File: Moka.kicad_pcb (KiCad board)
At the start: 2 copper layers, 60 x 60 mm, 66 parts, among them J1 CONN_02X03, J10 CONN_01X05, J2 GS2, J3 GS2, J4 GS2, J5 GS2, J6 GS2, J7 CONN_01X05, J8 CONN_01X05, J9 CONN_01X05, SW1 SW_Push, SW10 SW_Push, SW11 SW_Push, SW12 SW_Push, SW13 SW_Push, SW14 SW_Push, SW15 SW_Push, SW16 SW_Push, SW2 SW_Push, SW3 SW_Push, SW4 SW_Push, SW5 SW_Push, SW6 SW_Push, SW7 SW_Push, SW8 SW_Push, SW9 SW_Push, U1 ATMEGA328P-AU

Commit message: Design ok, first prototype batch ordered.
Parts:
- added logo1: Moka, Logos:Moka_20mm, B.Cu at (180.6, 128.2)
- added logo2: le labo, Logos:Le_labo_15mm, B.Cu at (151.2, 128.9)
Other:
- board text added: "6/2017"
- board text added: "lelabodutroisieme.fr"
- board text added: "v0.9"

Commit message: v0.95 ready for fabrication.
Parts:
- added D17: SK6812_MINI, Display_perso:SK6812-mini, F.Cu at (187.5, 132.5)
- D1: value Led_3535_addr -> D; footprint Display_perso:SK6812-mini -> Diodes_SMD:D_0603; moved to B.Cu
- D10, D11, D12, D13, D14, D15, D16, D2, D3, D4, D5, D6, D7, D8, D9: value Led_3535_addr -> SK6812_MINI
- J1: value CONN_02X03 -> Conn_02x03_Odd_Even; footprint Conn_perso:Pin_Header_Straight_2x03_Pitch2.54mm_SMD -> Connectors_perso:Pin_Header_Straight_2x03_Pitch2.54mm_SMD
- J10, J7, J8, J9: footprint Conn_perso:Connecteur_1x5_SMD -> Connectors_perso:Connecteur_1x5_SMD
- SW1, SW10, SW11, SW12, SW13, SW14, SW15, SW16, SW2, SW3, SW4, SW5, SW6, SW7, SW8, SW9: footprint Switches_perso:Pad_30 -> switches_perso:Pad_30
- logo1: footprint Logos:Moka_20mm -> logos:Moka_25mm
- logo2: footprint Logos:Le_labo_15mm -> logos:Le_labo_20mm
- moved J8 56.0 mm to (165.0, 138.0)
- moved D13 47.4 mm to (187.5, 117.5)
- moved D5 47.4 mm to (187.5, 87.5)
- moved D9 47.4 mm to (187.5, 102.5)
- moved J10 39.6 mm to (193.0, 110.0), turned to 90 degrees
- moved J9 39.6 mm to (165.0, 82.0), turned to 0 degrees
- moved D1 38.2 mm to (169.2, 114.8), turned to 315 degrees
- moved C3 37.1 mm to (190.1, 111.3), turned to 90 degrees
- moved C4 35.5 mm to (163.8, 135.0), turned to 0 degrees
- moved J2 35.0 mm to (180.1, 115.1), turned to 270 degrees
- moved C2 34.9 mm to (163.7, 84.9), turned to 0 degrees
- moved C5 33.8 mm to (140.0, 111.3), turned to 90 degrees
- moved J3 33.4 mm to (180.1, 112.6), turned to 270 degrees
- moved J4 32.1 mm to (180.1, 110.1), turned to 270 degrees
- moved J5 31.1 mm to (180.1, 107.5), turned to 270 degrees
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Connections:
- D1 pad 1: GND -> Net-(D1-Pad1)
- D1 pad 2: DIN -> INT
- D10 pad 1: GND -> Net-(D10-Pad1)
- D10 pad 2: Net-(D10-Pad2) -> GND
- D10 pad 3: +5V -> Net-(D10-Pad3)
- D10 pad 4: Net-(D10-Pad4) -> +5V
- D11 pad 1: GND -> Net-(D11-Pad1)
- D11 pad 2: Net-(D10-Pad4) -> GND
- D11 pad 3: +5V -> Net-(D10-Pad1)
- D11 pad 4: Net-(D11-Pad4) -> +5V
- D12 pad 1: GND -> Net-(D12-Pad1)
- D12 pad 2: Net-(D11-Pad4) -> GND
- D12 pad 3: +5V -> Net-(D11-Pad1)
- D12 pad 4: Net-(D12-Pad4) -> +5V
- D13 pad 1: GND -> Net-(D13-Pad1)
- D13 pad 2: Net-(D12-Pad4) -> GND
- D13 pad 3: +5V -> Net-(D12-Pad1)
- D13 pad 4: Net-(D13-Pad4) -> +5V
- D14 pad 1: GND -> Net-(D14-Pad1)
- D14 pad 2: Net-(D13-Pad4) -> GND
- D14 pad 3: +5V -> Net-(D13-Pad1)
- D14 pad 4: Net-(D14-Pad4) -> +5V
- D15 pad 1: GND -> Net-(D15-Pad1)
- D15 pad 2: Net-(D14-Pad4) -> GND
- D15 pad 3: +5V -> Net-(D14-Pad1)
- D15 pad 4: Net-(D15-Pad4) -> +5V
- D16 pad 1: GND -> Net-(D16-Pad1)
- D16 pad 2: Net-(D15-Pad4) -> GND
- D16 pad 3: +5V -> Net-(D15-Pad1)
- D16 pad 4: (no net) -> +5V
- D2 pad 1: GND -> Net-(D2-Pad1)
- D2 pad 2: Net-(D1-Pad4) -> GND
- D2 pad 3: +5V -> DIN
- D2 pad 4: Net-(D2-Pad4) -> +5V
- D3 pad 1: GND -> Net-(D3-Pad1)
- D3 pad 2: Net-(D2-Pad4) -> GND
- D3 pad 3: +5V -> Net-(D2-Pad1)
- D3 pad 4: Net-(D3-Pad4) -> +5V
- D4 pad 1: GND -> Net-(D4-Pad1)
- D4 pad 2: Net-(D3-Pad4) -> GND
- D4 pad 3: +5V -> Net-(D3-Pad1)
- D4 pad 4: Net-(D4-Pad4) -> +5V
- D5 pad 1: GND -> Net-(D5-Pad1)
- D5 pad 2: Net-(D4-Pad4) -> GND
- D5 pad 3: +5V -> Net-(D4-Pad1)
- D5 pad 4: Net-(D5-Pad4) -> +5V
- D6 pad 1: GND -> Net-(D6-Pad1)
- D6 pad 2: Net-(D5-Pad4) -> GND
- D6 pad 3: +5V -> Net-(D5-Pad1)
- D6 pad 4: Net-(D6-Pad4) -> +5V
- D7 pad 1: GND -> Net-(D7-Pad1)
- D7 pad 2: Net-(D6-Pad4) -> GND
- D7 pad 3: +5V -> Net-(D6-Pad1)
- D7 pad 4: Net-(D7-Pad4) -> +5V
- D8 pad 1: GND -> Net-(D8-Pad1)
- D8 pad 2: Net-(D7-Pad4) -> GND
- D8 pad 3: +5V -> Net-(D7-Pad1)
- D8 pad 4: Net-(D8-Pad4) -> +5V
- D9 pad 1: GND -> Net-(D10-Pad3)
- D9 pad 2: Net-(D8-Pad4) -> GND
- D9 pad 3: +5V -> Net-(D8-Pad1)
- D9 pad 4: Net-(D10-Pad2) -> +5V
- SW1 pad 1: BOUT1 -> BREAD1
- SW1 pad 2: BIN1 -> BCH1
- SW10 pad 1: BOUT2 -> BREAD2
- SW10 pad 2: BIN3 -> BCH3
- SW11 pad 1: BOUT3 -> BREAD3
- SW11 pad 2: BIN3 -> BCH3
- SW12 pad 1: BOUT4 -> BREAD4
- SW12 pad 2: BIN3 -> BCH3
- SW13 pad 1: BOUT1 -> BREAD1
- SW13 pad 2: BIN4 -> BCH4
- SW14 pad 1: BOUT2 -> BREAD2
- SW14 pad 2: BIN4 -> BCH4
- SW15 pad 1: BOUT3 -> BREAD3
- SW15 pad 2: BIN4 -> BCH4
- SW16 pad 1: BOUT4 -> BREAD4
- SW16 pad 2: BIN4 -> BCH4
- SW2 pad 1: BOUT2 -> BREAD2
- SW2 pad 2: BIN1 -> BCH1
- SW3 pad 1: BOUT3 -> BREAD3
- SW3 pad 2: BIN1 -> BCH1
- SW4 pad 1: BOUT4 -> BREAD4
- SW4 pad 2: BIN1 -> BCH1
- SW5 pad 1: BOUT1 -> BREAD1
- SW5 pad 2: BIN2 -> BCH2
- SW6 pad 1: BOUT2 -> BREAD2
- SW6 pad 2: BIN2 -> BCH2
- SW7 pad 1: BOUT3 -> BREAD3
- SW7 pad 2: BIN2 -> BCH2
- SW8 pad 1: BOUT4 -> BREAD4
- SW8 pad 2: BIN2 -> BCH2
- SW9 pad 1: BOUT1 -> BREAD1
- SW9 pad 2: BIN3 -> BCH3
- U1 pad 1: DIN -> BCH4
- U1 pad 10: BOUT3 -> ADDR2
- U1 pad 11: BOUT4 -> ADDR3
- U1 pad 12: ADDR0 -> ADDR4
- U1 pad 13: ADDR1 -> DIN
- U1 pad 14: ADDR2 -> Net-(D1-Pad1)
- U1 pad 2: BOUT1 -> ADDR0
- U1 pad 23: BIN1 -> BREAD1
- U1 pad 24: BIN2 -> BREAD2
- U1 pad 25: BIN3 -> BREAD3
- U1 pad 26: BIN4 -> BREAD4
- U1 pad 30: ADDR3 -> BCH1
- U1 pad 31: ADDR4 -> BCH2
- U1 pad 32: INT -> BCH3
- U1 pad 9: BOUT2 -> ADDR1
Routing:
- net GND: track 438.9 -> 514.0 mm, vias 56 -> 57
- net BOUT1: track 70.4 -> 0.00 mm, vias 7 -> 0
- net BCH1: track 0.00 -> 70.3 mm, vias 0 -> 1
- net Net-(D4-Pad4): track 69.7 -> 0.00 mm, vias 2 -> 0
- net Net-(D8-Pad4): track 67.4 -> 0.00 mm, vias 4 -> 0
- net BOUT4: track 67.0 -> 0.00 mm, vias 7 -> 0
- net BIN1: track 65.5 -> 0.00 mm, vias 3 -> 0
- net BIN4: track 62.9 -> 0.00 mm, vias 4 -> 0
- net BCH4: track 0.00 -> 61.3 mm, vias 0 -> 3
- net Net-(D10-Pad3): track 0.00 -> 60.8 mm, vias 0 -> 2
- net Net-(D12-Pad4): track 57.7 -> 0.00 mm, vias 2 -> 0
- net Net-(D5-Pad1): track 0.00 -> 55.7 mm, vias 0 -> 2
- net BOUT2: track 55.1 -> 0.00 mm, vias 5 -> 0
- net BOUT3: track 54.9 -> 0.00 mm, vias 7 -> 0
- net BCH3: track 0.00 -> 54.0 mm, vias 0 -> 1
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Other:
- board text added: "9/2017"
- board text added: "ADDR0"
- board text added: "ADDR1"
- board text added: "ADDR2"
- board text added: "ADDR3"
- board text added: "ADDR4"
- board text added: "MISO"
- board text added: "MOSI"
- board text added: "RST"
- board text added: "SCK"
- board text added: "v0.95"
- board text removed: "6/2017"
- board text removed: "addr 0"
- board text removed: "addr 1"
- board text removed: "addr 2"
- board text removed: "addr 3"
- board text removed: "addr 4"
- board text removed: "v0.9"

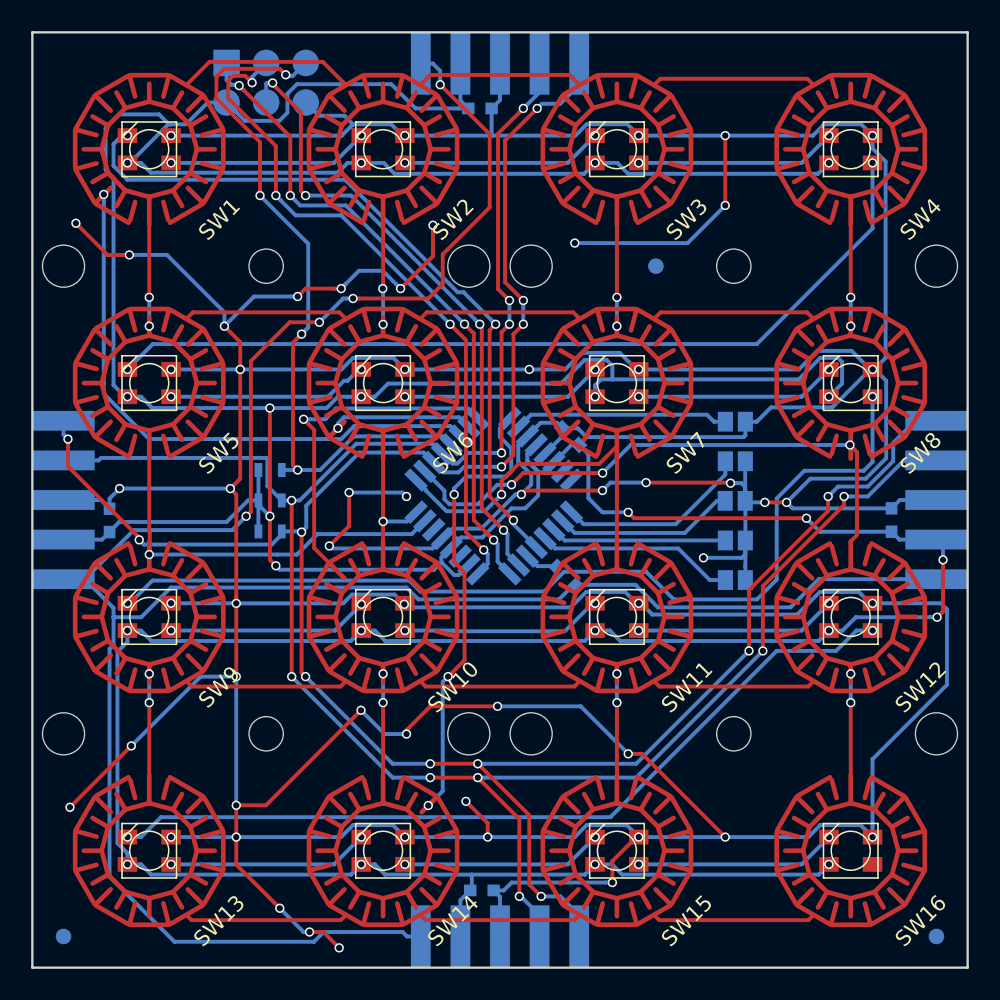
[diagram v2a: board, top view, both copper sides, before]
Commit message: Modified diode footprint on INT.
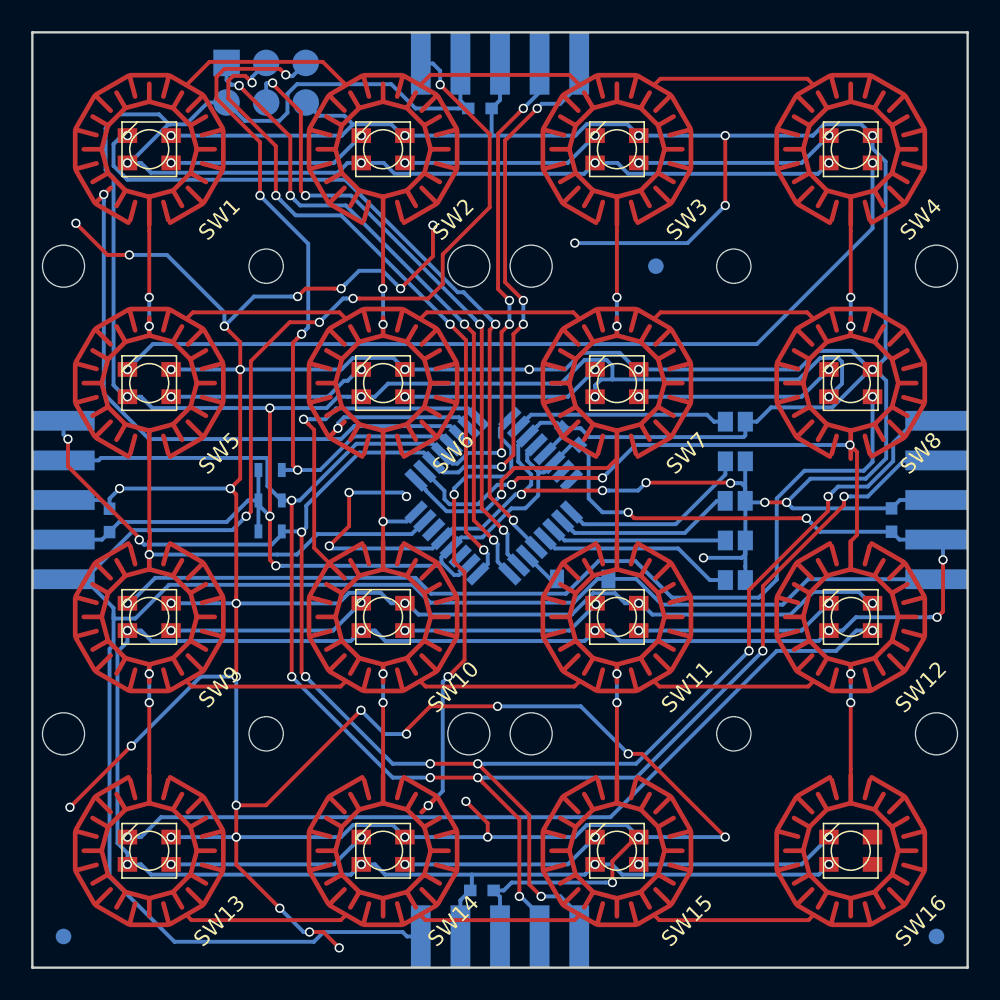
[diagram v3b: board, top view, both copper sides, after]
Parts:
- D1: footprint Diodes_SMD:D_0603 -> Diodes_SMD:D_SOD-123
- moved D1 1.13 mm to (170.3, 115.1), turned to 0 degrees
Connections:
- D17 pad 1: (no net) -> Net-(D17-Pad1)
- U1 pad 19: (no net) -> Net-(U1-Pad19)
- U1 pad 22: (no net) -> Net-(U1-Pad22)
- U1 pad 7: (no net) -> Net-(U1-Pad7)
- U1 pad 8: (no net) -> Net-(U1-Pad8)
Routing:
- net GND: track 514.0 -> 482.8 mm, vias 57 -> 56
- net Net-(D10-Pad3): track 60.8 -> 61.6 mm
- net INT: track 153.2 -> 153.7 mm

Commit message: Added missing via on last led raw GND.
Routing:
- net GND: vias 56 -> 57
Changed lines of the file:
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@@
     (links 858)
     (no_connects 721)
-    (area 134.924999 79.924999 195.075001 140.075001)
+    (area 131.680952 74.578618 198.319048 142.885)
     (thickness 1.6)
     (drawings 39)
-    (tracks 1033)
+    (tracks 1034)
     (zones 0)
     (modules 69)
@@
   (segment (start 137 112.54) (end 139.473 112.54) (width 0.25) (layer B.Cu) (net 1))
   (segment (start 139.473 112.54) (end 139.953 112.06) (width 0.25) (layer B.Cu) (net 1))
+  (via (at 188.9 131.625) (size 0.6) (drill 0.4) (layers F.Cu B.Cu) (net 2))
   (segment (start 148.081 116.632) (end 154.64 116.632) (width 0.25) (layer B.Cu) (net 2))
   (segment (start 154.64 116.632) (end 155.321 115.951) (width 0.25) (layer B.Cu) (net 2))
